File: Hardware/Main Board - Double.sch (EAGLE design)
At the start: 72 parts, among them J1 MICROMOD-2222-C, J10 MICRO-SD-PUSH-PUSH-EXT-PIN, J2 Vertical Qwiic Connector, J4 QWIIC_RIGHT_ANGLE, J5 CORTEX_JTAG_DEBUG_MINIMUM_PTH, J6 MICROMOD_FUNCTION_MAIN, J7 MICROMOD_FUNCTION_MAIN, Q1 3.1A/30V/105mΩ, U1 STG3856QTR, U2 MCP73831, U5 AP7361C-33

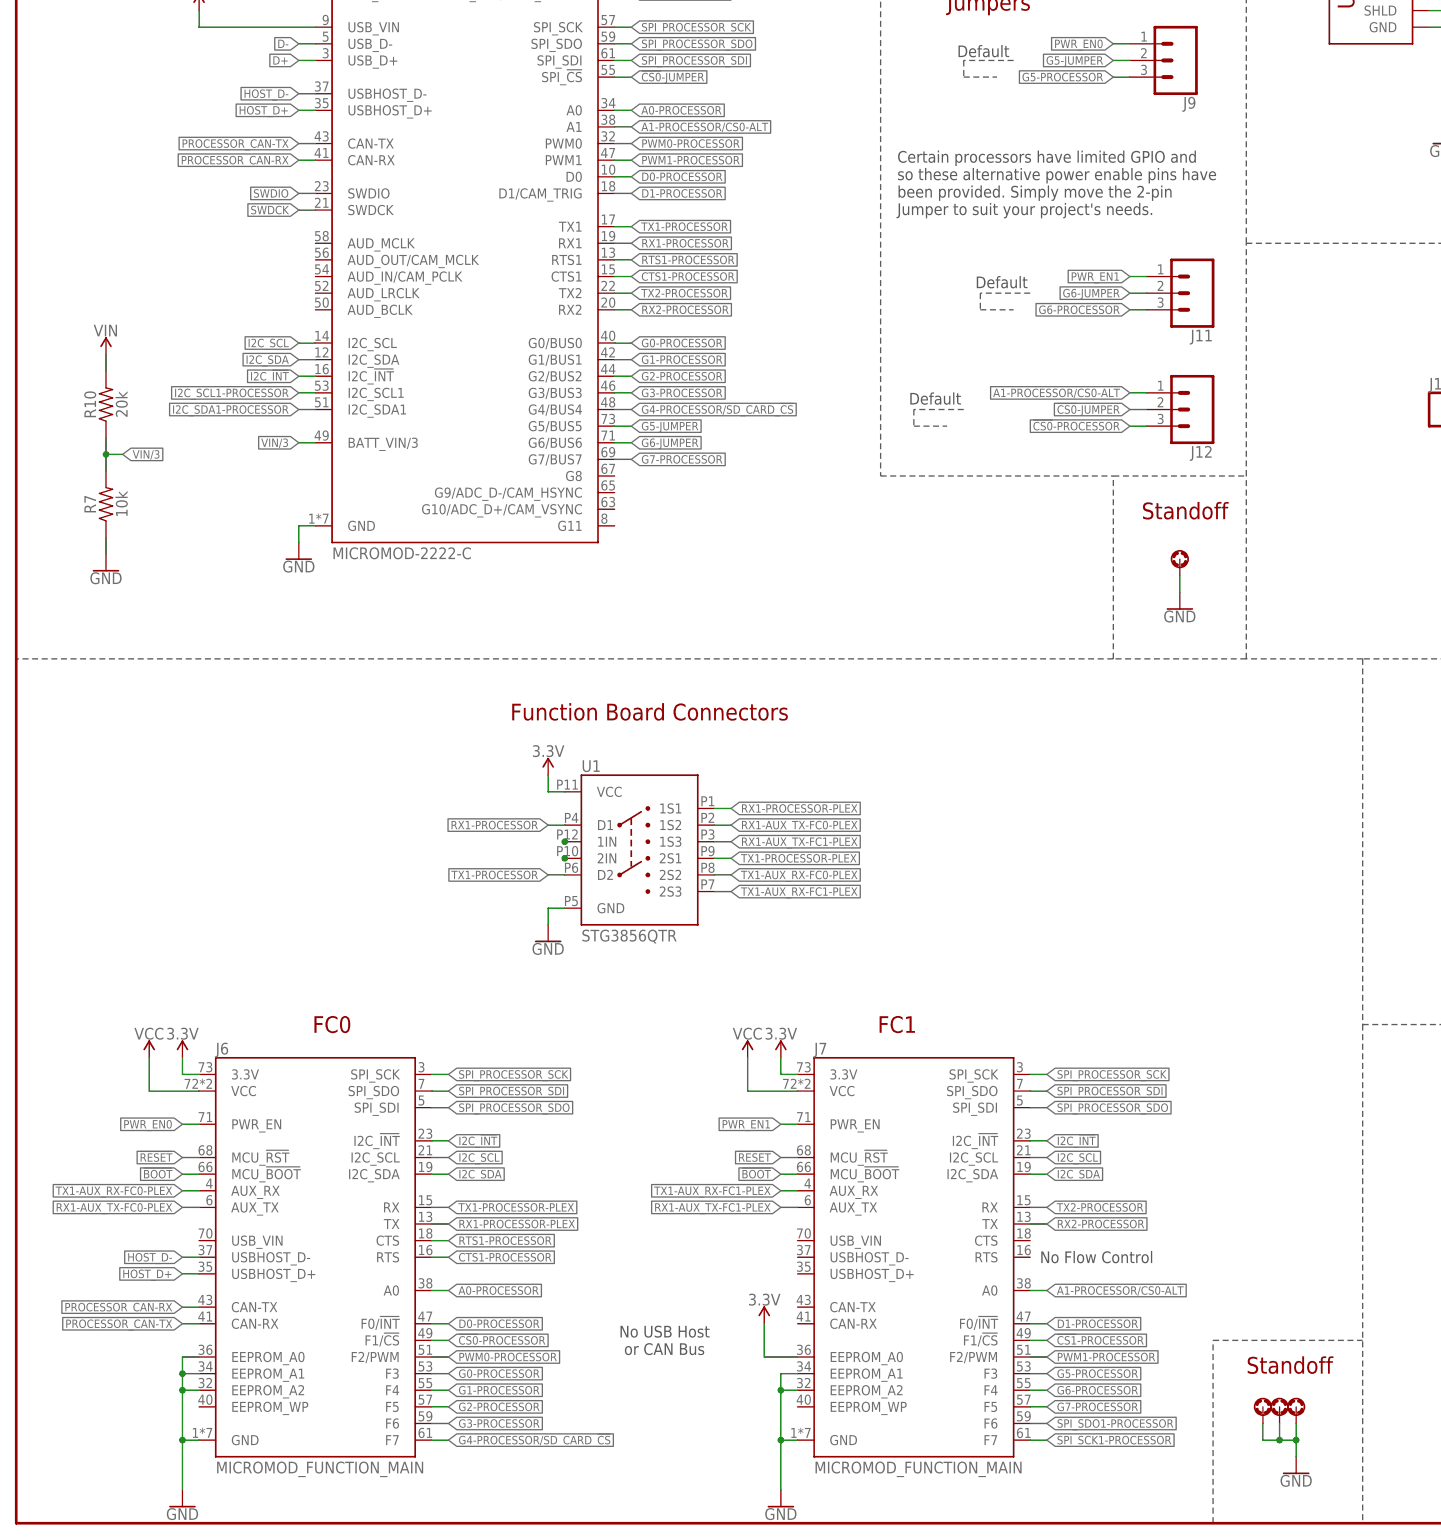
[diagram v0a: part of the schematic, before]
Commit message: Adds default state to plexer, includes new function card symbol with new plexing control pins
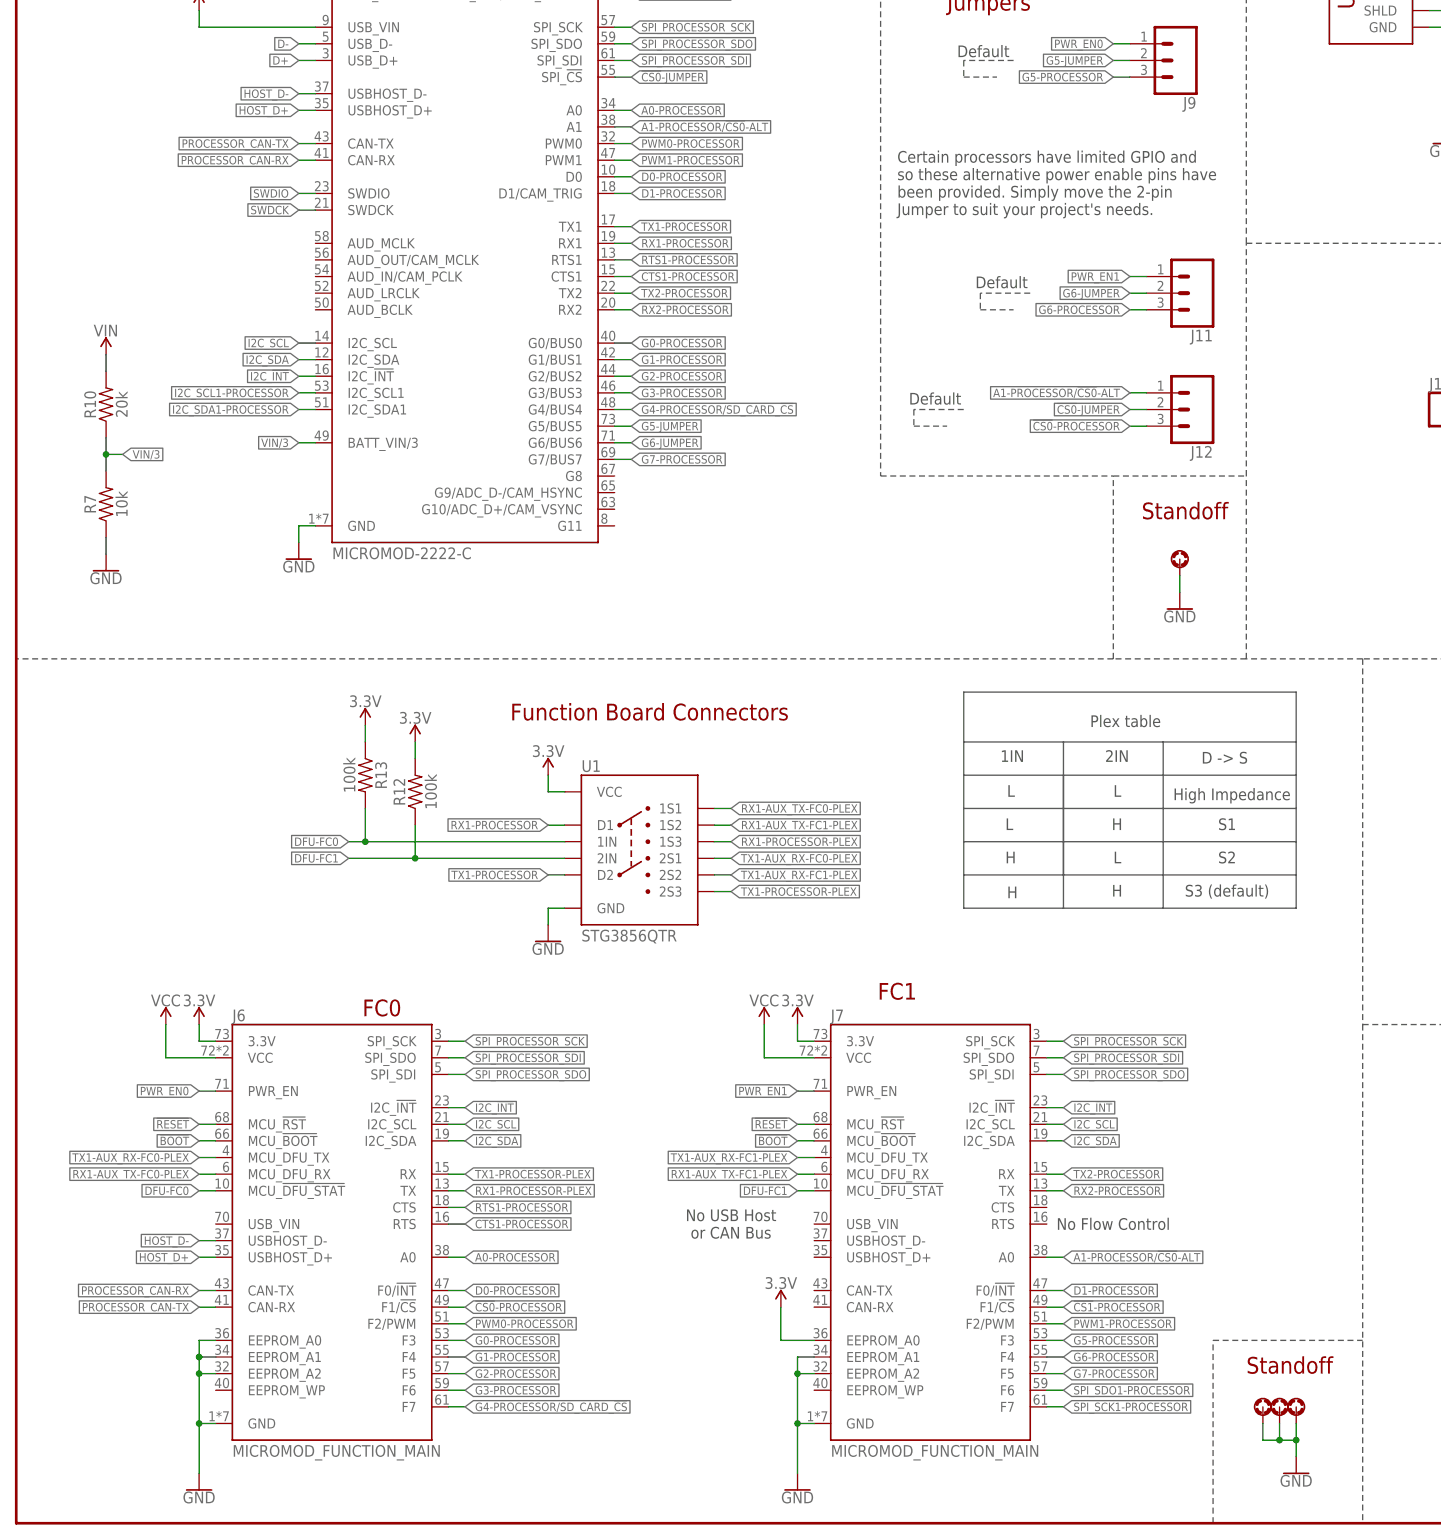
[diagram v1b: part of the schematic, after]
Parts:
- added R12, R13: 100k, SparkFun-Resistors:100KOHM-0603-1/10W-1%
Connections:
- net A1-PROCESSOR/CS0-ALT renamed A1-PROCESSOR/!CS0!-ALT
- removed net N$16: U1.1IN
- removed net N$17: U1.2IN
- new net DFU-FC0: J6.MCU_!DFU_STAT!, R13.2, U1.1IN
- new net DFU-FC1: J7.MCU_!DFU_STAT!, R12.1, U1.2IN
- net 3.3V: now also R12.2, R13.1
- net RX1-AUX_TX-FC0-PLEX: now also J6.MCU_DFU_RX, U1.1S1; no longer J6.AUX_TX, U1.1S2
- net RX1-AUX_TX-FC1-PLEX: now also J7.MCU_DFU_RX, U1.1S2; no longer J7.AUX_TX, U1.1S3
- net RX1-PROCESSOR-PLEX: now also U1.1S3; no longer U1.1S1
- net TX1-AUX_RX-FC0-PLEX: now also J6.MCU_DFU_TX, U1.2S1; no longer J6.AUX_RX, U1.2S2
- net TX1-AUX_RX-FC1-PLEX: now also J7.MCU_DFU_TX, U1.2S2; no longer J7.AUX_RX, U1.2S3
- net TX1-PROCESSOR-PLEX: now also U1.2S3; no longer U1.2S1
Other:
- note added: "1IN"
- note added: "2IN"
- note added: "D -> S"
- note added: "H"
- note added: "High Impedance"
- note added: "L"
- note added: "Plex table"
- note added: "S1"
- note added: "S2"
- note added: "S3 (default)"

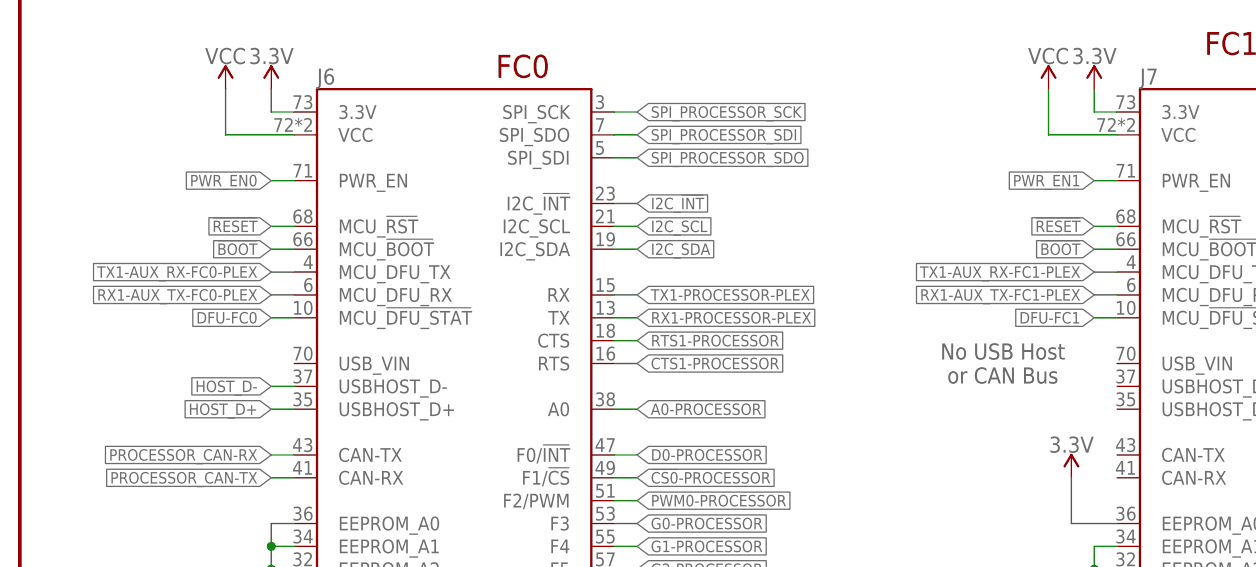
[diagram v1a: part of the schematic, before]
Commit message: Fixes swapped RX/TX
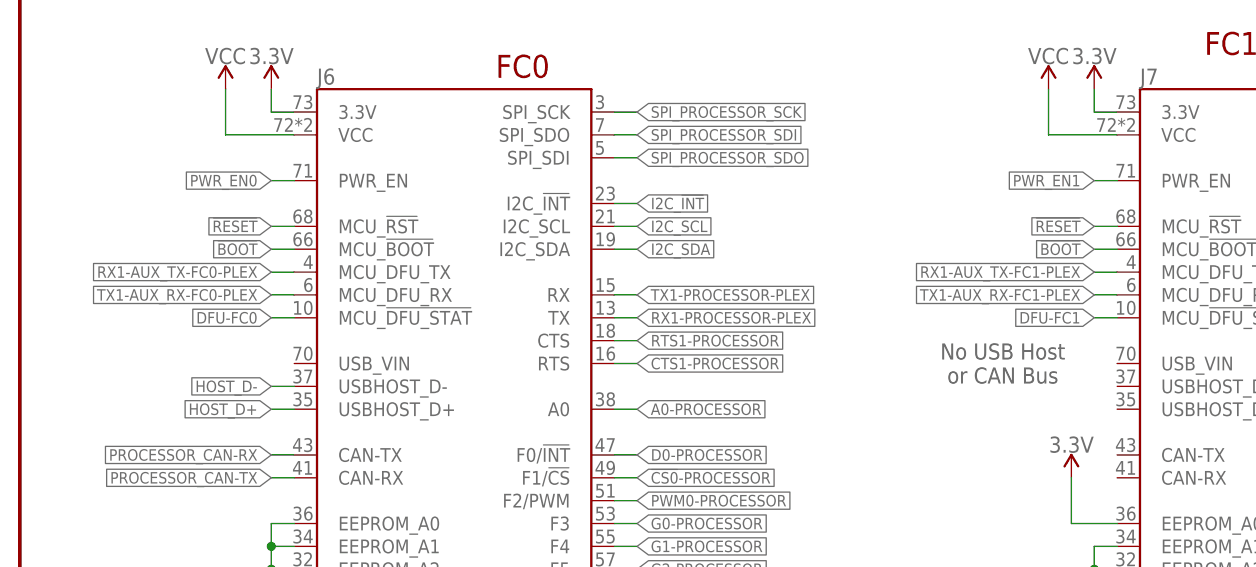
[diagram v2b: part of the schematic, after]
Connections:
- net RX1-AUX_TX-FC0-PLEX: now also J6.MCU_DFU_TX; no longer J6.MCU_DFU_RX
- net RX1-AUX_TX-FC1-PLEX: now also J7.MCU_DFU_TX; no longer J7.MCU_DFU_RX
- net TX1-AUX_RX-FC0-PLEX: now also J6.MCU_DFU_RX; no longer J6.MCU_DFU_TX
- net TX1-AUX_RX-FC1-PLEX: now also J7.MCU_DFU_RX; no longer J7.MCU_DFU_TX
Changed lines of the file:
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@@
 <net name="TX1-AUX_RX-FC0-PLEX" class="0">
-<segment>
-<wire x1="27.94" y1="55.88" x2="30.48" y2="55.88" width="0.1524" layer="91"/>
-<label x="27.94" y="55.88" size="1.27" layer="95" font="vector" rot="R180" xref="yes"/>
-<pinref part="J6" gate="J1" pin="MCU_DFU_TX"/>
-</segment>
 <segment>
 <wire x1="109.22" y1="101.6" x2="106.68" y2="101.6" width="0.1524" layer="91"/>
@@
 <pinref part="U1" gate="G$1" pin="2S1"/>
 </segment>
+<segment>
+<wire x1="27.94" y1="53.34" x2="30.48" y2="53.34" width="0.1524" layer="91"/>
+<label x="27.94" y="53.34" size="1.27" layer="95" font="vector" rot="R180" xref="yes"/>
+<pinref part="J6" gate="J1" pin="MCU_DFU_RX"/>
+</segment>
 </net>
 <net name="RX1-AUX_TX-FC1-PLEX" class="0">
-<segment>
-<wire x1="119.38" y1="53.34" x2="121.92" y2="53.34" width="0.1524" layer="91"/>
-<label x="119.38" y="53.34" size="1.27" layer="95" font="vector" rot="R180" xref="yes"/>
-<pinref part="J7" gate="J1" pin="MCU_DFU_RX"/>
-</segment>
 <segment>
 <wire x1="109.22" y1="106.68" x2="106.68" y2="106.68" width="0.1524" layer="91"/>
@@
 <pinref part="U1" gate="G$1" pin="1S2"/>
 </segment>
+<segment>
+<wire x1="119.38" y1="55.88" x2="121.92" y2="55.88" width="0.1524" layer="91"/>
+<label x="119.38" y="55.88" size="1.27" layer="95" font="vector" rot="R180" xref="yes"/>
+<pinref part="J7" gate="J1" pin="MCU_DFU_TX"/>
+</segment>
 </net>
 <net name="RX1-AUX_TX-FC0-PLEX" class="0">
-<segment>
-<wire x1="27.94" y1="53.34" x2="30.48" y2="53.34" width="0.1524" layer="91"/>
-<label x="27.94" y="53.34" size="1.27" layer="95" font="vector" rot="R180" xref="yes"/>
-<pinref part="J6" gate="J1" pin="MCU_DFU_RX"/>
-</segment>
 <segment>
 <wire x1="109.22" y1="109.22" x2="106.68" y2="109.22" width="0.1524" layer="91"/>
 <label x="109.22" y="109.22" size="1.27" layer="95" font="vector" xref="yes"/>
 <pinref part="U1" gate="G$1" pin="1S1"/>
+</segment>
+<segment>
+<wire x1="27.94" y1="55.88" x2="30.48" y2="55.88" width="0.1524" layer="91"/>
+<label x="27.94" y="55.88" size="1.27" layer="95" font="vector" rot="R180" xref="yes"/>
+<pinref part="J6" gate="J1" pin="MCU_DFU_TX"/>
 </segment>
 </net>
@@
 <net name="TX1-AUX_RX-FC1-PLEX" class="0">
 <segment>
-<wire x1="119.38" y1="55.88" x2="121.92" y2="55.88" width="0.1524" layer="91"/>
-<label x="119.38" y="55.88" size="1.27" layer="95" font="vector" rot="R180" xref="yes"/>
-<pinref part="J7" gate="J1" pin="MCU_DFU_TX"/>
-</segment>
-<segment>
 <wire x1="109.22" y1="99.06" x2="106.68" y2="99.06" width="0.1524" layer="91"/>
 <label x="109.22" y="99.06" size="1.27" layer="95" font="vector" xref="yes"/>
 <pinref part="U1" gate="G$1" pin="2S2"/>
 </segment>
+<segment>
+<wire x1="119.38" y1="53.34" x2="121.92" y2="53.34" width="0.1524" layer="91"/>
+<label x="119.38" y="53.34" size="1.27" layer="95" font="vector" rot="R180" xref="yes"/>
+<pinref part="J7" gate="J1" pin="MCU_DFU_RX"/>
+</segment>
 </net>

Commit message: Adds pull up resistors to i2c data lines
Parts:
- added I2C_PU: JUMPER-SMT_3_2-NC_TRACE_SILK, SparkFun-Jumpers:JUMPER-SMT_3_2-NC_TRACE_SILK
- added R14, R15: 2.2k, SparkFun-Resistors:2.2KOHM-0603-1/10W-1%
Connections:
- net DFU-FC0 renamed !DFU-FC0!
- net DFU-FC1 renamed !DFU-FC1!
- new net N$11: I2C_PU.3, R14.2
- new net N$13: I2C_PU.1, R15.2
- net 3.3V: now also I2C_PU.2
- net I2C_SCL: now also R15.1
- net I2C_SDA: now also R14.1
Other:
- moved on the sheet: J2, J4

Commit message: Updates cream and stop layers on uart-multiplexer
* Updates schematic
* Routes pullup jumper
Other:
- note added: "UART Multiplexer"
- moved on the sheet: 3V3_LED, 5V_LED, C10, C11, C12, C2, C5, C8, C9, D1, D3, D5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
